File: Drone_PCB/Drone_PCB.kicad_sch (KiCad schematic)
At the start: 59 parts, among them J1 Conn_01x04_Pin, J2 Conn_01x08_Socket, J3 Conn_01x05_Socket, J4 Conn_01x02_Socket, J5 Conn_01x02_Socket, J6 Conn_01x02_Socket, J7 Conn_01x02_Socket, J8 Conn_01x02_Socket, J9 USB_B_Micro, Q1 AO3400A, Q2 AO3400A, Q3 AO3400A, Q4 AO3400A, Q5 AO3400A, Q6 AO3400A, SW1 SW_Push, SW2 SW_SPST, U1 STM32F411RCT6, U2 AP2112K-3.3, U3 TP4056-42-ESOP8, U4 DW01A, Y1 26MHz

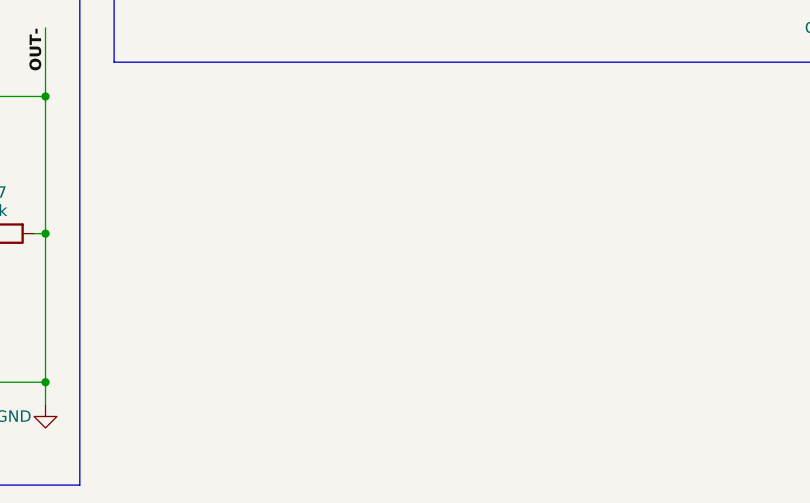
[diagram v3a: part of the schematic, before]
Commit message: Added Mounting Holers + Edges
Now PCB is almost ready in 3D terms
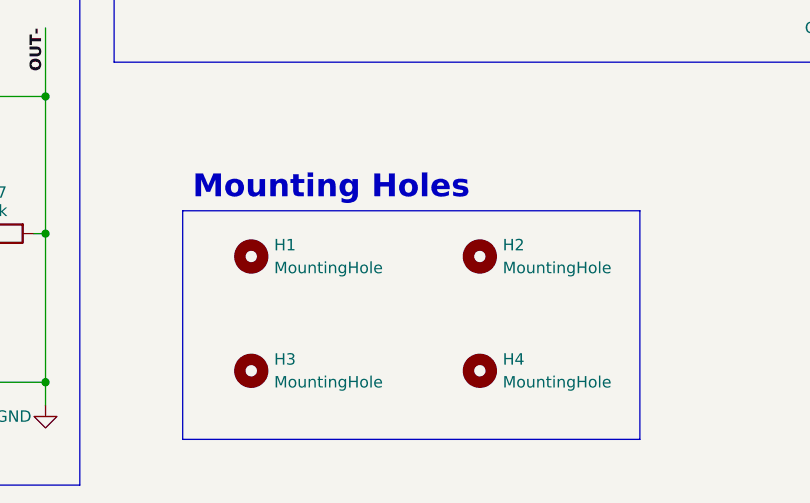
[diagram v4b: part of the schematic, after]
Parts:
- added H1, H2, H3, H4: MountingHole, MountingHole:MountingHole_2.2mm_M2, symbol Mechanical:MountingHole
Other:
- note added: "Mounting Holes"

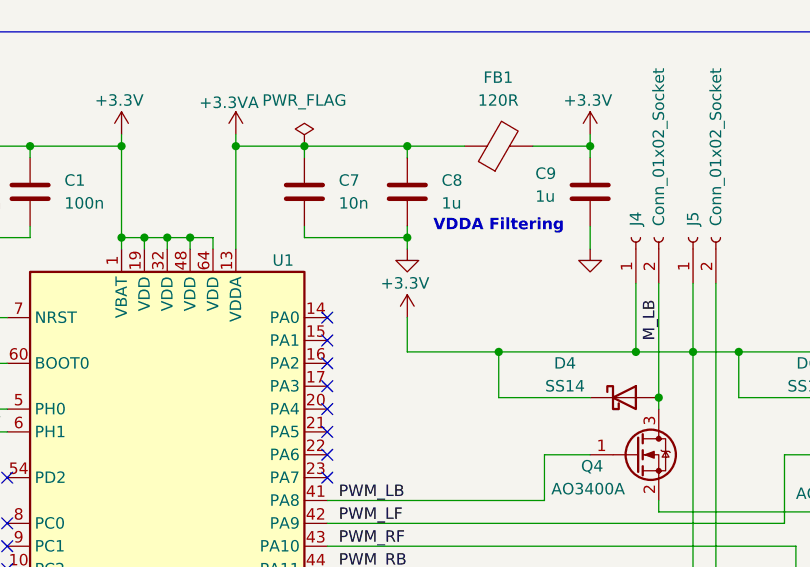
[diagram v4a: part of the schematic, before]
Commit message: Added GND routes
It should work okay now
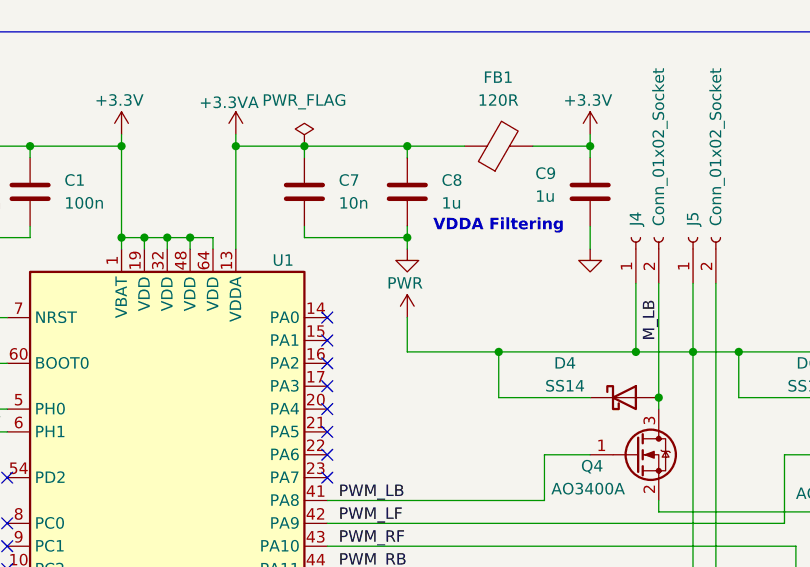
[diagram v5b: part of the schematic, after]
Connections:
- net +3.3V: no longer D4.1 (K), D5.1 (K), D6.1 (K), D7.1 (K), J4.1 (Pin_1), J5.1 (Pin_1), J6.1 (Pin_1), J7.1 (Pin_1)
- net PWR: now also D4.1 (K), D5.1 (K), D6.1 (K), D7.1 (K), J4.1 (Pin_1), J5.1 (Pin_1), J6.1 (Pin_1), J7.1 (Pin_1)
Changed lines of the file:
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@@
 			)
 		)
-		(property "Value" "+3.3V"
+		(property "Value" "PWR"
 			(at 211.836 46.99 0)
 			(effects

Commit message: Final routes
I guess it's okay now
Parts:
- removed Y1: 26MHz, Crystal:Crystal_SMD_HC49-SD, symbol Device:Crystal
- added Y1: 26MHz, Crystal:Crystal_SMD_3225-4Pin_3.2x2.5mm, symbol Device:Crystal_GND24
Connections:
- net GND: now also Y1.2, Y1.4
- net HSE_IN: now also Y1.1
- net HSE_OUT: now also Y1.3
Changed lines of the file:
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@@
 	)
 	(junction
+		(at 146.05 80.01)
+		(diameter 0)
+		(color 0 0 0 0)
+	)
+	(junction
 		(at 209.55 121.92)
 		(diameter 0)
@@
 	)
 	(junction
+		(at 139.7 80.01)
+		(diameter 0)
+		(color 0 0 0 0)
+	)
+	(junction
 		(at 71.12 138.43)
 		(diameter 0)
@@
 	(wire
 		(pts
+			(xy 146.05 66.04) (xy 146.05 64.77)
+		)
+		(stroke
+			(width 0)
+			(type default)
+		)
+	)
+	(wire
+		(pts
 			(xy 138.43 86.36) (xy 138.43 91.44)
 		)
@@
 	(wire
 		(pts
+			(xy 146.05 64.77) (xy 139.7 64.77)
+		)
+		(stroke
+			(width 0)
+			(type default)
+		)
+	)
+	(wire
+		(pts
 			(xy 29.21 148.59) (xy 29.21 154.94)
 		)
@@
 	(wire
 		(pts
+			(xy 146.05 76.2) (xy 146.05 80.01)
+		)
+		(stroke
+			(width 0)
+			(type default)
+		)
+	)
+	(wire
+		(pts
 			(xy 73.66 110.49) (xy 60.96 110.49)
 		)
@@
 	(wire
 		(pts
+			(xy 139.7 64.77) (xy 139.7 80.01)
+		)
+		(stroke
+			(width 0)
+			(type default)
+		)
+	)
+	(wire
+		(pts
 			(xy 115.57 99.06) (xy 143.51 99.06)
 		)
@@
 	(wire
 		(pts
+			(xy 139.7 80.01) (xy 146.05 80.01)
+		)
+		(stroke
+			(width 0)
+			(type default)
+		)
+	)
+	(wire
+		(pts
 			(xy 29.21 128.27) (xy 29.21 129.54)
 		)
@@
 	(wire
 		(pts
-			(xy 133.35 80.01) (xy 157.48 80.01)
+			(xy 133.35 80.01) (xy 139.7 80.01)
 		)
 		(stroke
@@
 	(wire
 		(pts
+			(xy 146.05 80.01) (xy 157.48 80.01)
+		)
+		(stroke
+			(width 0)
+			(type default)
+		)
+	)
+	(wire
+		(pts
 			(xy 185.42 41.91) (xy 185.42 43.18)
 		)
@@
 	(wire
 		(pts
-			(xy 151.13 71.12) (xy 157.48 71.12)
+			(xy 149.86 71.12) (xy 157.48 71.12)
 		)
 		(stroke
@@
 	(wire
 		(pts
-			(xy 133.35 71.12) (xy 143.51 71.12)
+			(xy 133.35 71.12) (xy 142.24 71.12)
 		)
 		(stroke
@@
 	)
 	(symbol
-		(lib_id "Device:Crystal")
-		(at 147.32 71.12 0)
-		(unit 1)
-		(exclude_from_sim no)
-		(in_bom yes)
-		(on_board yes)
-		(dnp no)
-		(fields_autoplaced yes)
-		(property "Reference" "Y1"
-			(at 147.32 63.5 0)
-			(effects
-				(font
-					(size 1.27 1.27)
-				)
-			)
-		)
-		(property "Value" "26MHz"
-			(at 147.32 66.04 0)
-			(effects
-				(font
-					(size 1.27 1.27)
-				)
-			)
-		)
-		(property "Footprint" "Crystal:Crystal_SMD_HC49-SD"
-			(at 147.32 71.12 0)
-			(effects
-				(font
-					(size 1.27 1.27)
-				)
-				(hide yes)
-			)
-		)
-		(property "Datasheet" "~"
-			(at 147.32 71.12 0)
-			(effects
-				(font
-					(size 1.27 1.27)
-				)
-				(hide yes)
-			)
-		)
-		(property "Description" "Two pin crystal"
-			(at 147.32 71.12 0)
-			(effects
-				(font
-					(size 1.27 1.27)
-				)
-				(hide yes)
-			)
-		)
-		(pin "2"
-		)
-		(pin "1"
-		)
-		(instances
-			(project ""
-				(path "/2c198202-91eb-4035-8605-360d42f3c3f5"
-					(reference "Y1")
-					(unit 1)
-				)
-			)
-		)
-	)
-	(symbol
 		(lib_id "Device:C")
 		(at 90.17 152.4 90)
@@
 		(on_board yes)
 		(dnp no)
-		(fields_autoplaced yes)
 		(property "Reference" "C11"
-			(at 137.16 73.6599 0)
+			(at 126.238 73.66 0)
 			(effects
 				(font
@@
 		)
 		(property "Value" "30p"
-			(at 137.16 76.1999 0)
+			(at 126.238 76.2 0)
 			(effects
 				(font
@@
 					(unit 1)
 				)
+			)
+		)
+	)
+	(symbol
+		(lib_id "Device:Crystal_GND24")
+		(at 146.05 71.12 0)
+		(unit 1)
+		(exclude_from_sim no)
+		(in_bom yes)
+		(on_board yes)
+		(dnp no)
+		(property "Reference" "Y1"
+			(at 147.574 66.294 0)
+			(effects
+				(font
+					(size 1.27 1.27)
+				)
+			)
+		)
+		(property "Value" "26MHz"
+			(at 149.606 76.2 0)
+			(effects
+				(font
+					(size 1.27 1.27)
+				)
+			)
+		)
+		(property "Footprint" "Crystal:Crystal_SMD_3225-4Pin_3.2x2.5mm"
+			(at 146.05 71.12 0)
+			(effects
+				(font
+					(size 1.27 1.27)
+				)
+				(hide yes)
+			)
+		)
+		(property "Datasheet" "~"
+			(at 146.05 71.12 0)
+			(effects
+				(font
+					(size 1.27 1.27)
+				)
+				(hide yes)
+			)
+		)
+		(property "Description" "Four pin crystal, GND on pins 2 and 4"
+			(at 146.05 71.12 0)
+			(effects
+				(font
+					(size 1.27 1.27)
+				)
+				(hide yes)
+			)
+		)
+		(pin "4"
+		)
+		(pin "2"
+		)
+		(pin "1"
+		)
+		(pin "3"
+		)
+		(instances
+			(project ""
+				(path "/2c198202-91eb-4035-8605-360d42f3c3f5"
+					(reference "Y1")
+					(unit 1)
+				)
